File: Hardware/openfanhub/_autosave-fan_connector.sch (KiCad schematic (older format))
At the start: 6 parts, among them M1 Fan_4pin, Q4 Q_PMOS_DGS

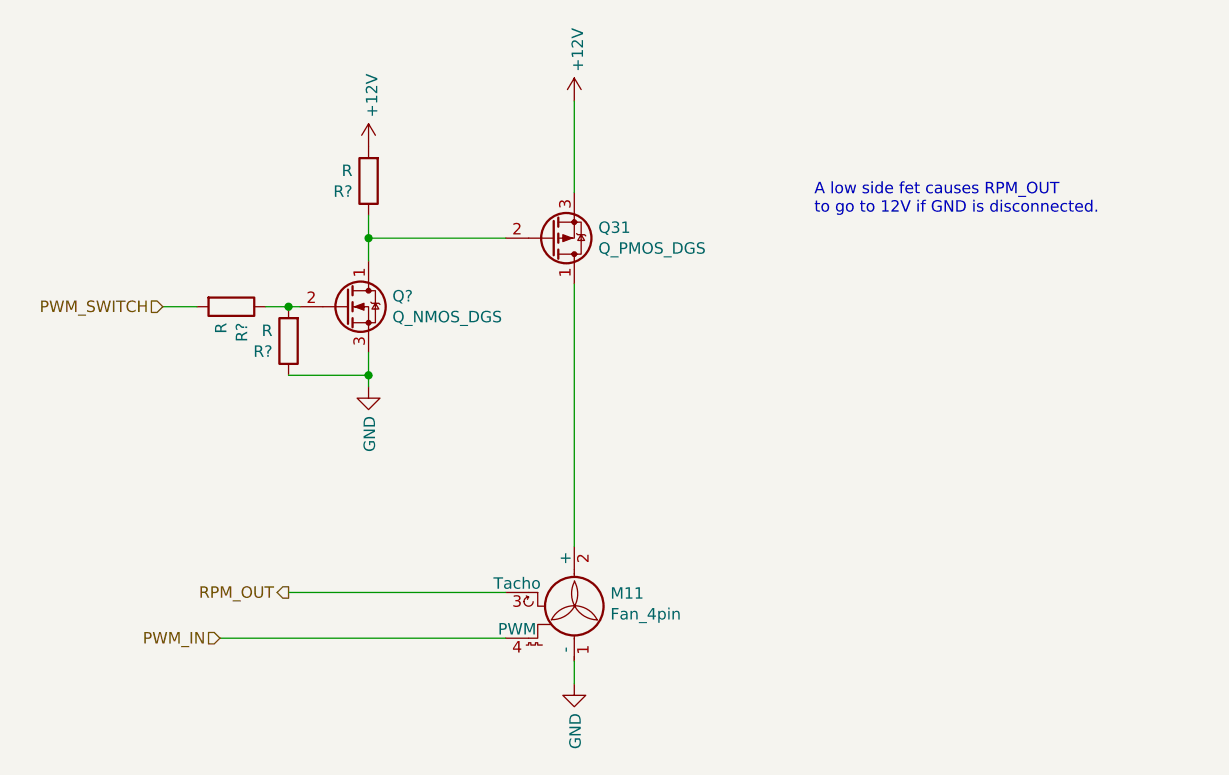
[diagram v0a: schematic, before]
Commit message: Fix switch to deactivate fan
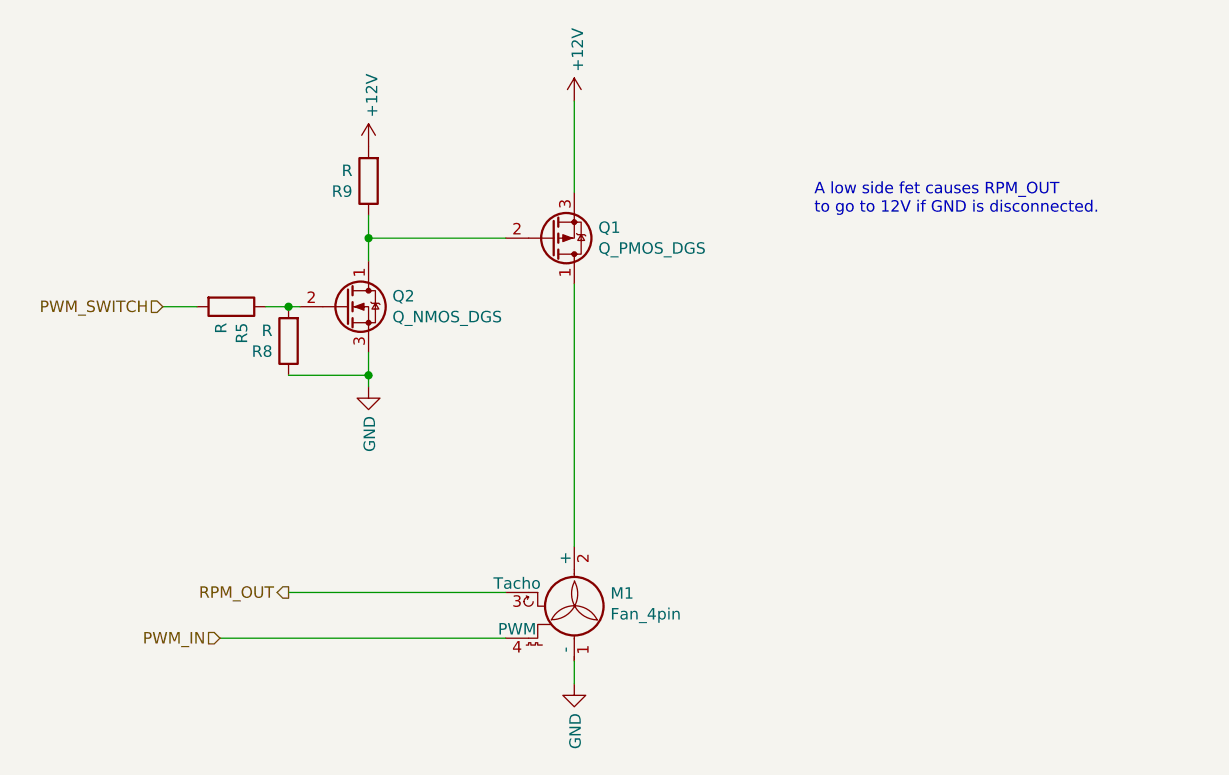
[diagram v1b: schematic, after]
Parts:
- gave numbers to parts that had none: 4
